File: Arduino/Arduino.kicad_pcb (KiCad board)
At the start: 2 copper layers, 98 parts, among them J1 Barrel_Jack_Switch, J11 USB_C_Receptacle_USB2.0, J12 USB_B, J13 Conn_01x04, J14 Screw_Terminal_01x12, J15 Conn_01x01, J16 Conn_01x01, J17 Conn_01x01, J18 Conn_01x01, J19 Pin, J2 Vcc, J20 Bt_ext, J21 Pin, J22 Bt_ext, J23 Pin, J24 Pin, J3 Conn_01x03, J8 ICSP, J9 Digital, K1 G5LE-1, K2 G5LE-1, K3 G5LE-1, K4 G5LE-1, Q3 SS8050, Q4 SS8050, Q5 SS8050, Q6 SS8050, SW2 Button, SW3 Button, U1 ATmega328P-P, U2 AMS1117-5.0, U3 CH340G, Y1 16MHz, Y2 12Mhz

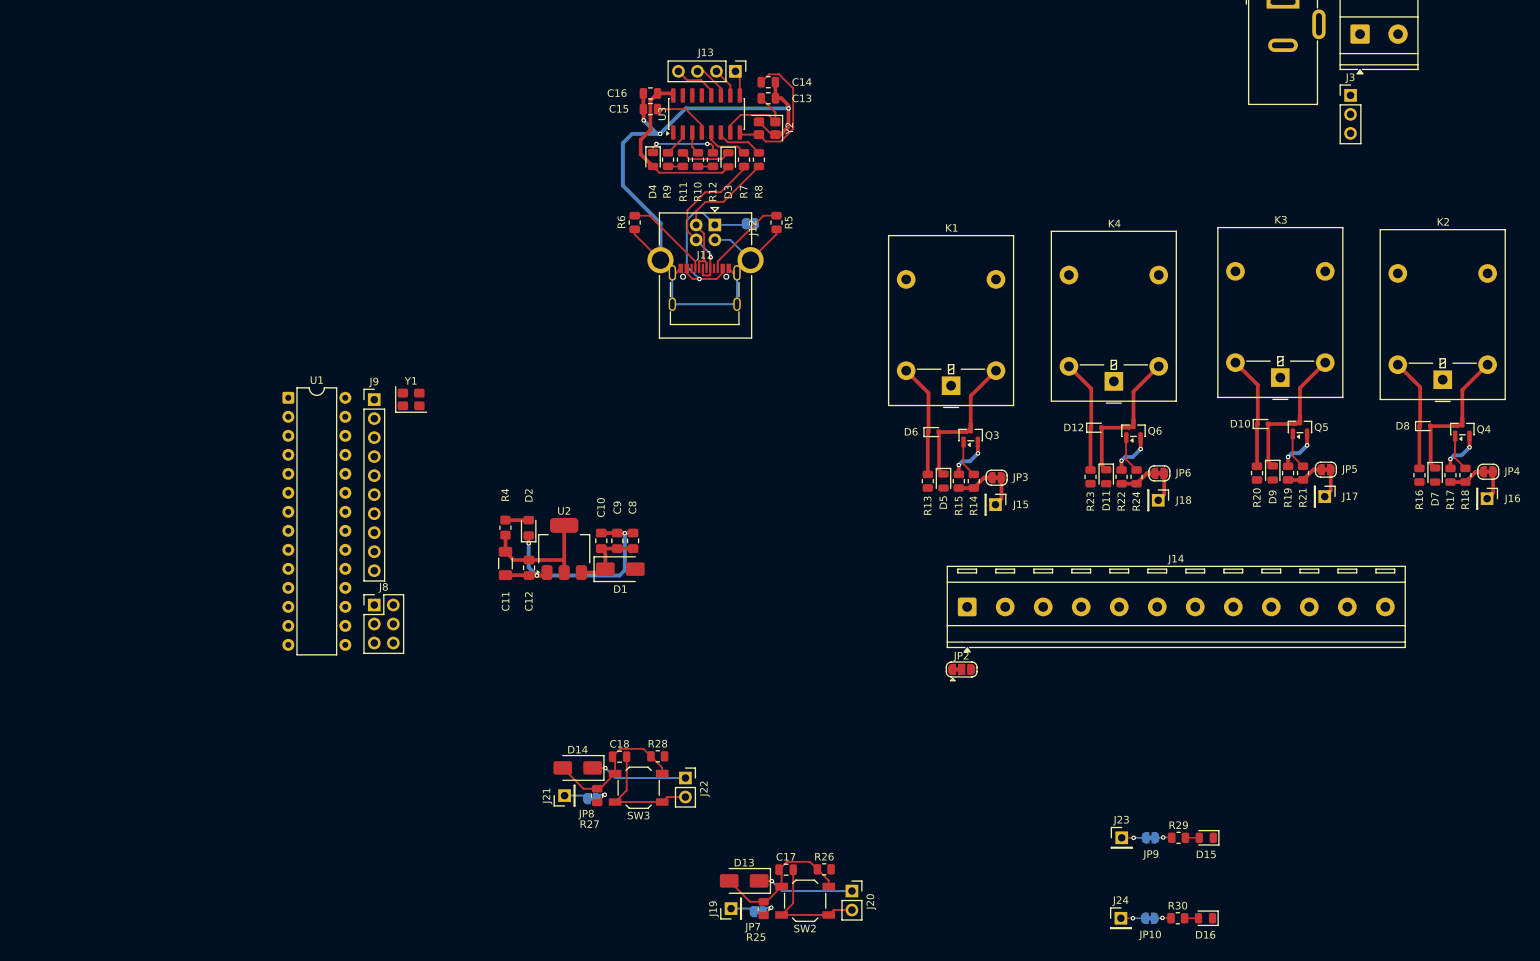
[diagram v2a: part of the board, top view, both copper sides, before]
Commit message: Added all components to arduino pcb.
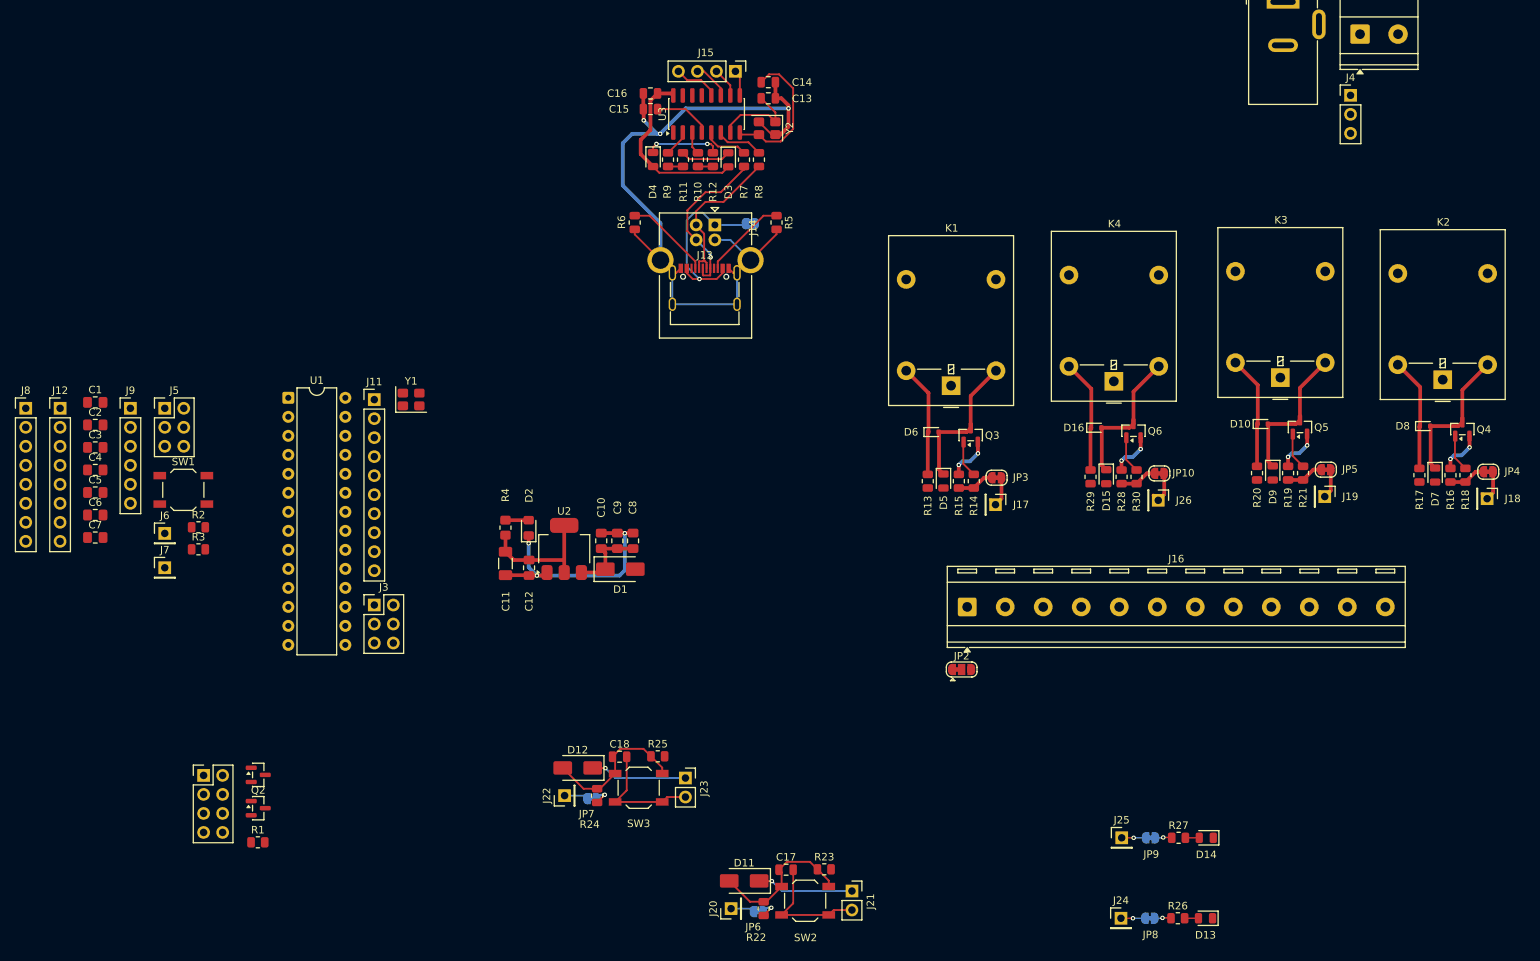
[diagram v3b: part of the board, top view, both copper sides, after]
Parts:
- added C1: 100n, Capacitor_SMD:C_0805_2012Metric_Pad1.18x1.45mm_HandSolder, F.Cu at (61.5, 72.1)
- added C2: 100n, Capacitor_SMD:C_0805_2012Metric_Pad1.18x1.45mm_HandSolder, F.Cu at (61.5, 75.1)
- added C3: 100n, Capacitor_SMD:C_0805_2012Metric_Pad1.18x1.45mm_HandSolder, F.Cu at (61.5, 78.1)
- added C4: 100n, Capacitor_SMD:C_0805_2012Metric_Pad1.18x1.45mm_HandSolder, F.Cu at (61.5, 81.1)
- added C5: 22p, Capacitor_SMD:C_0805_2012Metric_Pad1.18x1.45mm_HandSolder, F.Cu at (61.5, 84.2)
- added C6: 100n, Capacitor_SMD:C_0805_2012Metric_Pad1.18x1.45mm_HandSolder, F.Cu at (61.5, 87.2)
- added C7: 22p, Capacitor_SMD:C_0805_2012Metric_Pad1.18x1.45mm_HandSolder, F.Cu at (61.5, 90.2)
- added J10: I2C, Connector_PinHeader_2.54mm:PinHeader_2x04_P2.54mm_Vertical, F.Cu at (76.0, 122.0)
- added J12: Digital, Connector_PinHeader_2.54mm:PinHeader_1x08_P2.54mm_Vertical, F.Cu at (56.8, 72.9)
- added J5: Servo, Connector_PinHeader_2.54mm:PinHeader_2x03_P2.54mm_Vertical, F.Cu at (70.8, 72.9)
- added J6: Conn_01x01, Connector_PinHeader_2.54mm:PinHeader_1x01_P2.54mm_Vertical, F.Cu at (70.8, 89.6)
- added J7: Conn_01x01, Connector_PinHeader_2.54mm:PinHeader_1x01_P2.54mm_Vertical, F.Cu at (70.8, 94.2)
- added J8: Digital, Connector_PinHeader_2.54mm:PinHeader_1x08_P2.54mm_Vertical, F.Cu at (52.2, 72.9)
- added J9: Digital, Connector_PinHeader_2.54mm:PinHeader_1x06_P2.54mm_Vertical, F.Cu at (66.2, 72.9)
- added Q1: SS8050, Package_TO_SOT_SMD:SOT-23, F.Cu at (83.3, 121.9)
- added Q2: SS8050, Package_TO_SOT_SMD:SOT-23, F.Cu at (83.3, 126.3)
- added R1: 10k, Resistor_SMD:R_0805_2012Metric, F.Cu at (83.2, 130.9)
- added R2: 1k, Resistor_SMD:R_0805_2012Metric, F.Cu at (75.3, 88.8)
- added R3: 10k, Resistor_SMD:R_0805_2012Metric, F.Cu at (75.3, 91.8)
- added SW1: Reset, Button_Switch_SMD:SW_SPST_TL3342, F.Cu at (73.2, 83.8)
- JP10: renamed from JP6; value ~ -> A
- JP3, JP4, JP5: value ~ -> A
- R13: value 1k -> 10k
- R14: value 10k -> 1k
- renumbered D13 to D11, D14 to D12, D16 to D13, D15 to D14, D11 to D15, D12 to D16, J9 to J11, J11 to J13, J12 to J14, J13 to J15, J14 to J16, J15 to J17, J16 to J18, J17 to J19, J19 to J20, J20 to J21, J21 to J22, J22 to J23, J23 to J25, J18 to J26, J8 to J3, J3 to J4, JP7 to JP6, JP8 to JP7, JP10 to JP8, R17 to R16, R16 to R17, R25 to R22, R26 to R23, R27 to R24, R28 to R25, R30 to R26, R29 to R27, R22 to R28, R23 to R29, R24 to R30
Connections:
- C17 pad 1: Net-(D1001-A) -> Net-(D11-A)
- C17 pad 2: /GND -> GND
- C18 pad 1: Net-(D1001-A) -> Net-(D12-A)
- C18 pad 2: /GND -> GND
- D10 pad 1: /12V -> /Reles/Rele 1/12V
- D10 pad 2: Net-(D1001-K) -> Net-(D10-A)
- D11 pad 1: Net-(D1001-K) -> Net-(D11-K)
- D11 pad 2: Net-(D1001-A) -> Net-(D11-A)
- D12 pad 1: Net-(D1001-K) -> Net-(D12-K)
- D12 pad 2: Net-(D1001-A) -> Net-(D12-A)
- D13 pad 1: /GND -> GND
- D13 pad 2: Net-(D1001-A) -> Net-(D13-A)
- D14 pad 1: /GND -> GND
- D14 pad 2: Net-(D1001-A) -> Net-(D14-A)
- D15 pad 1: Net-(D1001-K) -> Net-(D15-K)
- D15 pad 2: Net-(D1001-A) -> Net-(D15-A)
- D16 pad 1: /12V -> /Reles/Rele 1/12V
- D16 pad 2: Net-(D1001-K) -> Net-(D15-K)
- D3 pad 1: Net-(D1001-K) -> Net-(D3-K)
- D3 pad 2: /Vcc -> +5V
- D4 pad 1: Net-(D1002-K) -> Net-(D4-K)
- D4 pad 2: /Vcc -> +5V
- D5 pad 1: Net-(D1001-K) -> Net-(D5-K)
- D5 pad 2: Net-(D1001-A) -> Net-(D5-A)
- D6 pad 1: /12V -> /Reles/Rele 1/12V
- D6 pad 2: Net-(D1001-K) -> Net-(D5-K)
- D7 pad 1: Net-(D1001-K) -> Net-(D7-K)
- D7 pad 2: Net-(D1001-A) -> Net-(D7-A)
- D8 pad 1: /12V -> /Reles/Rele 1/12V
- D8 pad 2: Net-(D1001-K) -> Net-(D7-K)
- D9 pad 1: Net-(D1001-K) -> Net-(D10-A)
- D9 pad 2: Net-(D1001-A) -> Net-(D9-A)
- J17 pad 1: /INPUT -> 5
- J18 pad 1: /INPUT -> 7
- J19 pad 1: /INPUT -> 8
- J20 pad 1: /OUT -> 9
- J21 pad 1: Net-(D1001-K) -> Net-(D11-K)
- J21 pad 2: /GND -> GND
- J22 pad 1: /OUT -> 3
- J23 pad 1: Net-(D1001-K) -> Net-(D12-K)
- J23 pad 2: /GND -> GND
- J24 pad 1: /IN -> 11
- J25 pad 1: /IN -> 13
- J26 pad 1: /INPUT -> 4
- JP10 pad 1: /INPUT -> 4
- JP10 pad 2: Net-(JP1001-B) -> Net-(JP10-B)
- JP3 pad 1: /INPUT -> 5
- JP3 pad 2: Net-(JP1001-B) -> Net-(JP3-B)
- JP4 pad 1: /INPUT -> 7
- JP4 pad 2: Net-(JP1001-B) -> Net-(JP4-B)
- JP5 pad 1: /INPUT -> 8
- JP5 pad 2: Net-(JP1001-B) -> Net-(JP5-B)
- JP6 pad 1: /OUT -> 9
- JP6 pad 2: Net-(JP1001-B) -> Net-(JP6-B)
- JP7 pad 1: /OUT -> 3
- JP7 pad 2: Net-(JP1001-B) -> Net-(JP7-B)
- JP8 pad 1: /IN -> 11
- JP8 pad 2: Net-(JP1001-B) -> Net-(JP8-B)
- JP9 pad 1: /IN -> 13
- JP9 pad 2: Net-(JP1001-B) -> Net-(JP9-B)
- K1 pad 1: /COM -> /Reles/Rele 2/COM
- K1 pad 2: Net-(D1001-K) -> Net-(D5-K)
- K1 pad 3: /NA -> /Reles/Rele 2/NA
- K1 pad 4: /NF -> /Reles/Rele 2/NF
- K1 pad 5: /12V -> /Reles/Rele 1/12V
- K2 pad 1: /COM -> /Reles/Rele 3/COM
- K2 pad 2: Net-(D1001-K) -> Net-(D7-K)
- K2 pad 3: /NA -> /Reles/Rele 3/NA
- K2 pad 4: /NF -> /Reles/Rele 3/NF
- K2 pad 5: /12V -> /Reles/Rele 1/12V
- K3 pad 1: /COM -> /Reles/Rele 4/COM
- K3 pad 2: Net-(D1001-K) -> Net-(D10-A)
- K3 pad 3: /NA -> /Reles/Rele 4/NA
- K3 pad 4: /NF -> /Reles/Rele 4/NF
- K3 pad 5: /12V -> /Reles/Rele 1/12V
- K4 pad 1: /COM -> /Reles/Rele 1/COM
- K4 pad 2: Net-(D1001-K) -> Net-(D15-K)
- K4 pad 3: /NA -> /Reles/Rele 1/NA
- K4 pad 4: /NF -> /Reles/Rele 1/NF
- K4 pad 5: /12V -> /Reles/Rele 1/12V
- Q3 pad 1: Net-(Q1001-B) -> Net-(Q3-B)
- Q3 pad 2: /GND -> GND
- Q3 pad 3: Net-(D1001-K) -> Net-(D5-K)
- Q4 pad 1: Net-(Q1001-B) -> Net-(Q4-B)
- Q4 pad 2: /GND -> GND
- Q4 pad 3: Net-(D1001-K) -> Net-(D7-K)
- Q5 pad 1: Net-(Q1001-B) -> Net-(Q5-B)
- Q5 pad 2: /GND -> GND
- Q5 pad 3: Net-(D1001-K) -> Net-(D10-A)
- Q6 pad 1: Net-(Q1001-B) -> Net-(Q6-B)
- Q6 pad 2: /GND -> GND
- Q6 pad 3: Net-(D1001-K) -> Net-(D15-K)
- R13 pad 1: /12V -> Net-(JP3-B)
- R13 pad 2: Net-(D1001-A) -> GND
- R14 pad 1: Net-(JP1001-B) -> /Reles/Rele 1/12V
- R14 pad 2: Net-(Q1001-B) -> Net-(D5-A)
- R15 pad 1: Net-(JP1001-B) -> Net-(JP3-B)
- R15 pad 2: /GND -> Net-(Q3-B)
- R16 pad 1: Net-(JP1001-B) -> Net-(JP4-B)
- R16 pad 2: /GND -> GND
- R17 pad 1: /12V -> /Reles/Rele 1/12V
- R17 pad 2: Net-(D1001-A) -> Net-(D7-A)
- R18 pad 1: Net-(JP1001-B) -> Net-(JP4-B)
- R18 pad 2: Net-(Q1001-B) -> Net-(Q4-B)
- R19 pad 1: Net-(JP1001-B) -> Net-(JP5-B)
- R19 pad 2: /GND -> GND
- R20 pad 1: /12V -> /Reles/Rele 1/12V
- R20 pad 2: Net-(D1001-A) -> Net-(D9-A)
- R21 pad 1: Net-(JP1001-B) -> Net-(JP5-B)
- R21 pad 2: Net-(Q1001-B) -> Net-(Q5-B)
- R22 pad 1: Net-(JP1001-B) -> Net-(JP6-B)
- R22 pad 2: Net-(D1001-A) -> Net-(D11-A)
- R23 pad 1: Net-(D1001-A) -> Net-(D11-A)
- R23 pad 2: /Vcc -> +5V
- R24 pad 1: Net-(JP1001-B) -> Net-(JP7-B)
- R24 pad 2: Net-(D1001-A) -> Net-(D12-A)
- R25 pad 1: Net-(D1001-A) -> Net-(D12-A)
- R25 pad 2: /Vcc -> +5V
- R26 pad 1: Net-(JP1001-B) -> Net-(JP8-B)
- R26 pad 2: Net-(D1001-A) -> Net-(D13-A)
- R27 pad 1: Net-(JP1001-B) -> Net-(JP9-B)
- R27 pad 2: Net-(D1001-A) -> Net-(D14-A)
- R28 pad 1: Net-(JP1001-B) -> Net-(JP10-B)
- R28 pad 2: /GND -> GND
- R29 pad 1: /12V -> /Reles/Rele 1/12V
- R29 pad 2: Net-(D1001-A) -> Net-(D15-A)
- R30 pad 1: Net-(JP1001-B) -> Net-(JP10-B)
- R30 pad 2: Net-(Q1001-B) -> Net-(Q6-B)
- SW2 pad 1: /GND -> GND
- SW2 pad 2: Net-(D1001-A) -> GND
- SW3 pad 1: /GND -> GND
- SW3 pad 2: Net-(D1001-A) -> GND
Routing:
- net Net-(D1001-K): track 110.2 -> 0.00 mm, vias 2 -> 0
- net (no net): track 0.00 -> 72.3 mm
- net /12V: track 60.5 -> 0.00 mm
- net /GND: track 56.6 -> 0.00 mm, vias 8 -> 0
- net GND: track 133.5 -> 184.1 mm, vias 6 -> 14
- net /Reles/Rele 1/12V: track 0.00 -> 45.4 mm
- net Net-(D1001-A): track 44.5 -> 0.00 mm
- net Net-(JP1001-B): track 30.8 -> 0.00 mm, vias 4 -> 0
- net /Vcc: track 24.3 -> 0.00 mm
- net +5V: track 0.00 -> 24.3 mm
- net Net-(Q1001-B): track 20.8 -> 0.00 mm
- net /INPUT: track 20.8 -> 0.00 mm
- net Net-(D7-K): track 0.00 -> 19.4 mm
- net Net-(D5-K): track 0.00 -> 19.4 mm
- net Net-(D10-A): track 0.00 -> 19.4 mm
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
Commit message: Added all components to arduino pcb.
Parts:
- J12: moved to B.Cu
- J8: value Digital -> Power
- moved J12 376.2 mm to (432.5, 92.3), turned to 90 degrees
- moved C6 366.4 mm to (426.6, 117.5), turned to -90 degrees
- moved J9 360.0 mm to (419.8, 140.6), turned to 90 degrees
- moved J8 351.3 mm to (396.9, 140.6), turned to 90 degrees
- moved U1 342.9 mm to (426.7, 120.5), turned to -90 degrees
- moved J3 333.4 mm to (431.8, 113.4)
- moved J11 312.6 mm to (410.6, 92.3), turned to -90 degrees
- moved SW1 283.6 mm to (353.2, 128.7), turned to 90 degrees
- moved R2 282.1 mm to (355.3, 122.5), turned to 90 degrees
- moved R3 279.8 mm to (353.4, 122.5), turned to 90 degrees
- moved C11 277.6 mm to (393.4, 110.4)
- moved C12 277.6 mm to (396.5, 111.0)
- moved C9 277.6 mm to (408.3, 107.4)
- moved R4 277.6 mm to (393.4, 105.6)
- moved C10 277.6 mm to (406.1, 107.4)
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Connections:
- SW1 pad 2: GND -> Net-(R2-Pad1)
- SW2 pad 2: GND -> Net-(D11-A)
- SW3 pad 2: GND -> Net-(D12-A)
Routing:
- net (no net): track 72.3 -> 31.5 mm
- net Net-(D11-A): track 0.00 -> 20.4 mm
- net Net-(D12-A): track 0.00 -> 20.4 mm
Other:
- board outline added: 98 x 98 mm

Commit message: First version from PCB schematic.
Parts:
- removed the JP3 at (187.0, 52.4)
- added JP1: A, Jumper:SolderJumper-2_P1.3mm_Bridged2Bar_RoundedPad1.0x1.5mm, B.Cu at (190.0, 107.8)
- added JP4: A, Jumper:SolderJumper-2_P1.3mm_Bridged_RoundedPad1.0x1.5mm, F.Cu at (165.6, 79.4)
- added RV1: 100k, Potentiometer_THT:Potentiometer_Bourns_3296W_Vertical, F.Cu at (192.4, 105.2)
- C13, C14, C15, C16, C17, C18: footprint Capacitor_SMD:C_0805_2012Metric -> Capacitor_SMD:C_0805_2012Metric_Pad1.18x1.45mm_HandSolder
- D10, D16, D6, D8: value 1N4148WT -> 1N4007; footprint Diode_SMD:D_SOD-523 -> Diode_SMD:D_SMA
- J16: footprint TerminalBlock_RND:TerminalBlock_RND_205-00297_1x12_P5.08mm_Horizontal -> TerminalBlock_Phoenix:TerminalBlock_Phoenix_PT-1,5-12-5.0-H_1x12_P5.00mm_Horizontal
- JP3: renamed from JP2; moved to B.Cu
- R1, R10, R11, R12, R13, R14, R15, R16, R17, R18, R19, R2, R20, R21, R22, R23, R24, R25, R26, R27, R28, R29, R3, R30, R5, R6, R7, R8, R9: footprint Resistor_SMD:R_0805_2012Metric -> Resistor_SMD:R_0805_2012Metric_Pad1.20x1.40mm_HandSolder
- moved C8 294.7 mm to (115.9, 117.7), turned to -90 degrees
- moved D1 291.1 mm to (117.6, 114.0), turned to 180 degrees
- moved C9 290.5 mm to (118.0, 117.7), turned to -90 degrees
- moved C10 286.2 mm to (120.2, 117.7), turned to -90 degrees
- moved U2 276.2 mm to (125.1, 116.7), turned to -90 degrees
- moved D2 266.9 mm to (129.9, 119.5), turned to -90 degrees
- moved C12 266.7 mm to (129.8, 114.1), turned to 90 degrees
- moved R4 260.7 mm to (133.0, 119.5), turned to 90 degrees
- moved C11 260.4 mm to (133.0, 114.7), turned to 90 degrees
- moved R2 248.2 mm to (107.2, 129.2)
- moved R3 248.2 mm to (105.3, 129.2)
- moved SW1 248.2 mm to (105.2, 135.3)
- moved D13 248.0 mm to (185.7, 140.1)
- moved D14 248.0 mm to (192.7, 140.2)
- moved J24 248.0 mm to (185.7, 128.8)
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- renumbered JP9 to JP10, JP10 to JP11, JP1 to JP2, JP4 to JP5, JP5 to JP6, JP6 to JP7, JP7 to JP8, JP8 to JP9
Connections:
- net /Regulador de Tensao/5V renamed /Regulador de Tensao/+5V
- net /Reles/Rele 1/12V renamed /Reles/Rele 1/+12V
- J16 pad 1: /Reles/Rele 4/NF -> /Reles/Rele 1/NA
- J16 pad 10: /Reles/Rele 1/NF -> /Reles/Rele 4/NA
- J16 pad 11: /Reles/Rele 1/COM -> /Reles/Rele 4/COM
- J16 pad 12: /Reles/Rele 1/NA -> /Reles/Rele 4/NF
- J16 pad 2: /Reles/Rele 4/COM -> /Reles/Rele 1/COM
- J16 pad 3: /Reles/Rele 4/NA -> /Reles/Rele 1/NF
- J16 pad 4: /Reles/Rele 3/NF -> /Reles/Rele 2/NA
- J16 pad 5: /Reles/Rele 3/COM -> /Reles/Rele 2/COM
- J16 pad 6: /Reles/Rele 3/NA -> /Reles/Rele 2/NF
- J16 pad 7: /Reles/Rele 2/NF -> /Reles/Rele 3/NA
- J16 pad 8: /Reles/Rele 2/COM -> /Reles/Rele 3/COM
- J16 pad 9: /Reles/Rele 2/NA -> /Reles/Rele 3/NF
- J2 pad 1: GND -> /Regulador de Tensao/Vin
- J2 pad 2: /Regulador de Tensao/Vin -> GND
- J5 pad 1: 5 -> 6
- J5 pad 2: 6 -> 5
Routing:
- net GND: track 184.1 -> 555.7 mm, vias 14 -> 29
- net +5V: track 24.3 -> 284.4 mm, vias 0 -> 6
- net 12: track 0.00 -> 205.8 mm
- net +12V: track 10.6 -> 179.8 mm, vias 0 -> 4
- net 11: track 3.20 -> 169.3 mm
- net 13: track 3.20 -> 158.0 mm, vias 1 -> 3
- net Reset: track 0.00 -> 119.2 mm, vias 0 -> 7
- net /CH340/DTR: track 0.00 -> 115.9 mm, vias 0 -> 6
- net A5: track 0.00 -> 109.7 mm, vias 0 -> 7
- net A4: track 0.00 -> 99.7 mm, vias 0 -> 7
- net TX: track 2.00 -> 97.5 mm, vias 0 -> 4
- net 3: track 3.17 -> 94.5 mm, vias 0 -> 1
- net Aref: track 0.00 -> 87.0 mm
- net /Reles/Rele 1/+12V: track 45.4 -> 130.1 mm
- net 5: track 5.19 -> 89.6 mm, vias 0 -> 2
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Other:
- board size 98 x 98 mm -> 98 x 116.3 mm
- board text added: "Q1"

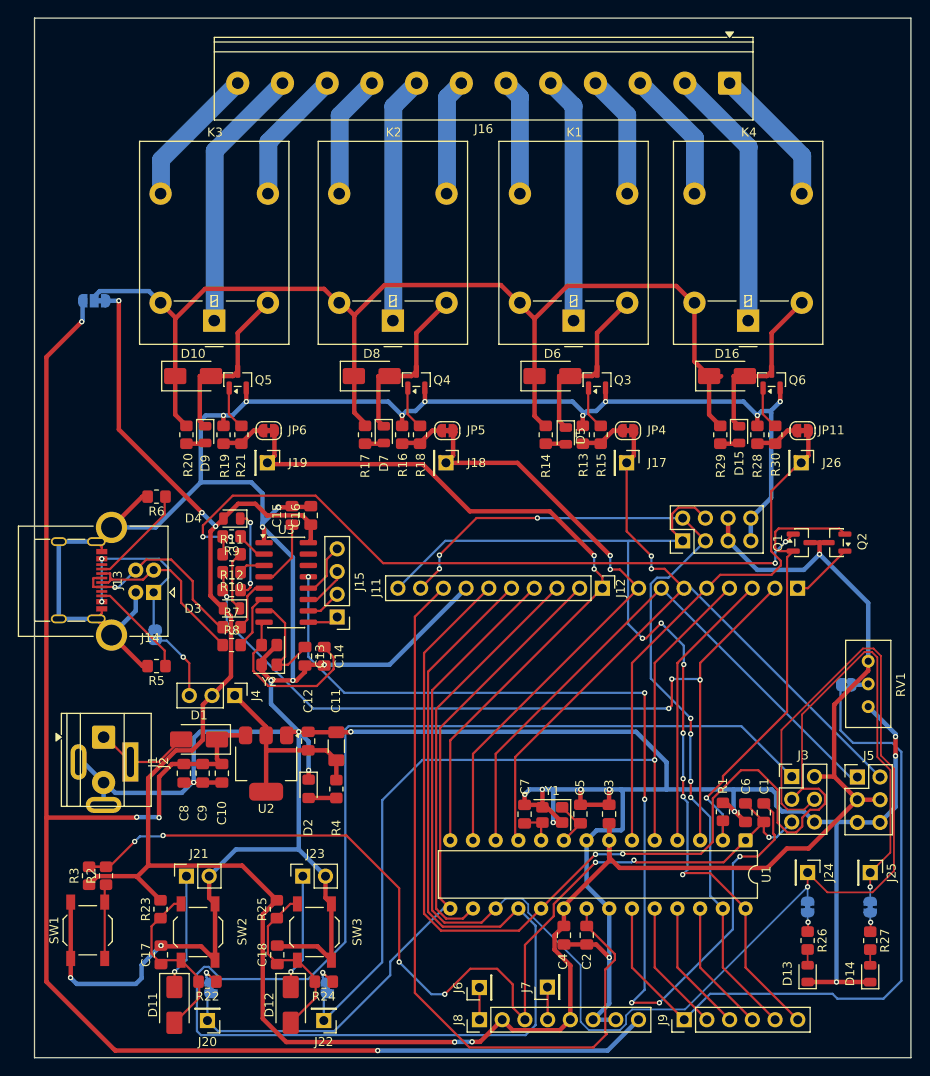
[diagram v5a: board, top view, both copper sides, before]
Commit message: Final version of arduino board.
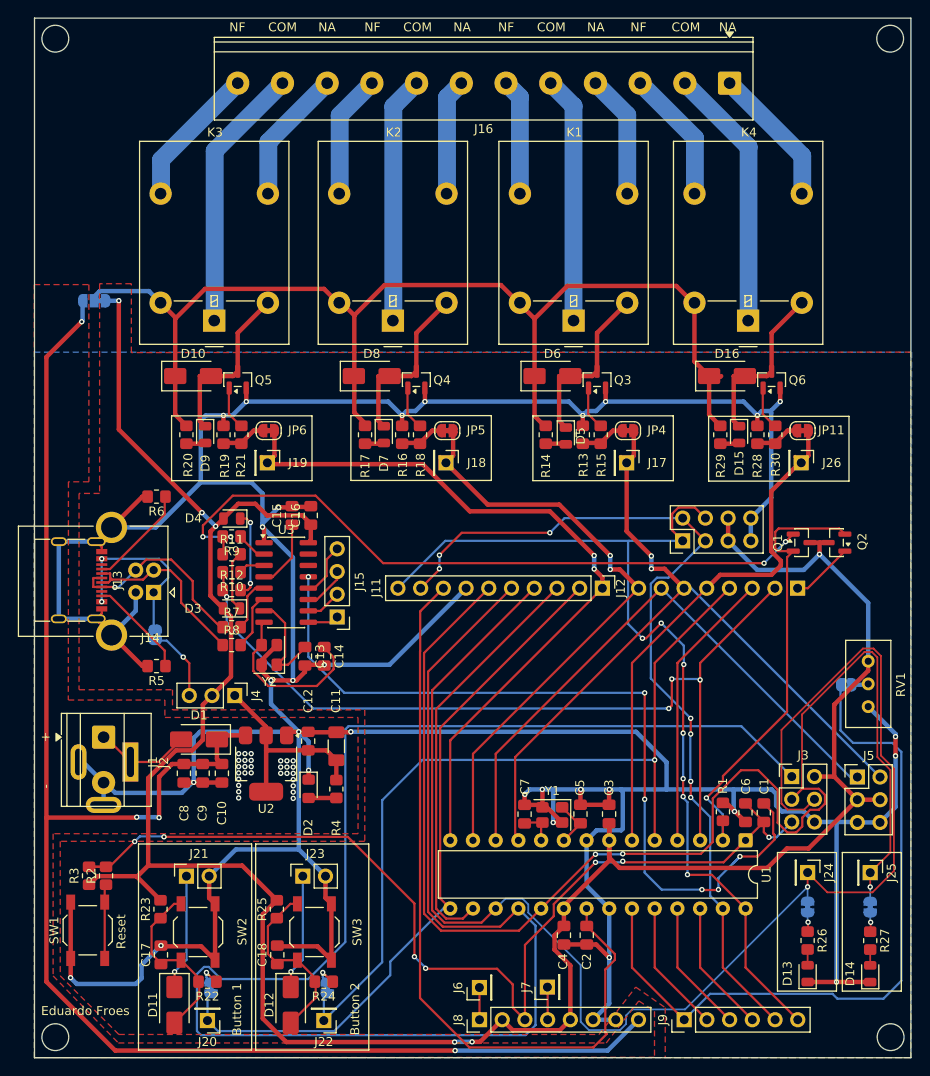
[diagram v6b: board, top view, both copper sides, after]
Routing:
- net /CH340/DTR: track 115.9 -> 92.4 mm
- net Reset: track 119.2 -> 115.4 mm
- net A5: track 109.7 -> 108.8 mm
- net RX1: track 80.0 -> 79.3 mm
- net GND: vias 29 -> 58
- added copper zone on F.Cu, net +12V
- added copper zone on F.Cu, net +5V
- added copper zone on B.Cu, net GND
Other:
- outline, holes or cut-outs redrawn
- board text added: "+"
- board text added: "-"
- board text added: "Ala Negra Technologies ©"
- board text added: "Button 1"
- board text added: "Button 2"
- board text added: "COM"
- board text added: "Eduardo Froes"
- board text added: "NA"
- board text added: "NF"
- board text added: "Reset"
